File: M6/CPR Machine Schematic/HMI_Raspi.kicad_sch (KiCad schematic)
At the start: 15 parts, among them J10 Stop Button Port, J11 Go Button Port, J9 Laser Port, Q3 T2N7002BK,LM, Q6 T2N7002BK,LM, Q7 T2N7002BK,LM

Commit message: Final PCB
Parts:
- J9: footprint Connector_PinHeader_2.54mm:PinHeader_1x02_P2.54mm_Vertical -> TerminalBlock:TerminalBlock_MaiXu_MX126-5.0-02P_1x02_P5.00mm; digikey (none) -> 277-1667-ND; now in the parts list
- R6: value TEMP kOhm -> 0 Ohm; footprint Resistor_SMD:R_1206_3216Metric -> Resistor_SMD:R_1206_3216Metric_Pad1.30x1.75mm_HandSolder; digikey (none) -> RMCF1206ZT0R00CT-ND
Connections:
- net +5V: no longer R6.2
- net at J9.2 (Pin_2): now also R6.2; no longer R6.1
- new net +3.3V: R6.1
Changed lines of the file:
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@@
+	(wire
+		(pts
+			(xy 153.67 91.44) (xy 146.05 91.44)
+		)
+		(stroke
+			(width 0)
+			(type default)
+		)
+	)
+	(wire
+		(pts
+			(xy 78.74 63.5) (xy 81.28 63.5)
+		)
+		(stroke
+			(width 0)
+			(type default)
+		)
+	)
+	(wire
+		(pts
+			(xy 142.24 86.36) (xy 153.67 86.36)
+		)
+		(stroke
+			(width 0)
+			(type default)
+		)
+	)
+	(wire
+		(pts
+			(xy 129.54 59.69) (xy 130.81 59.69)
+		)
+		(stroke
+			(width 0)
+			(type default)
+		)
+	)
+	(wire
+		(pts
+			(xy 146.05 52.07) (xy 153.67 52.07)
+		)
+		(stroke
+			(width 0)
+			(type default)
+		)
+	)
+	(wire
+		(pts
+			(xy 88.9 63.5) (xy 90.17 63.5)
+		)
+		(stroke
+			(width 0)
+			(type default)
+		)
+	)
+	(wire
+		(pts
+			(xy 146.05 91.44) (xy 146.05 93.98)
+		)
+		(stroke
+			(width 0)
+			(type default)
+		)
+	)
+	(wire
+		(pts
+			(xy 78.74 64.77) (xy 78.74 63.5)
+		)
+		(stroke
+			(width 0)
+			(type default)
+		)
+	)
 	(wire
 		(pts
 			(xy 97.79 52.07) (xy 97.79 53.34)
-		)
-		(stroke
-			(width 0)
-			(type default)
-		)
-	)
-	(wire
-		(pts
-			(xy 153.67 91.44) (xy 146.05 91.44)
-		)
-		(stroke
-			(width 0)
-			(type default)
-		)
-	)
-	(wire
-		(pts
-			(xy 78.74 63.5) (xy 81.28 63.5)
-		)
-		(stroke
-			(width 0)
-			(type default)
-		)
-	)
-	(wire
-		(pts
-			(xy 142.24 86.36) (xy 153.67 86.36)
-		)
-		(stroke
-			(width 0)
-			(type default)
-		)
-	)
-	(wire
-		(pts
-			(xy 129.54 59.69) (xy 130.81 59.69)
-		)
-		(stroke
-			(width 0)
-			(type default)
-		)
-	)
-	(wire
-		(pts
-			(xy 146.05 52.07) (xy 153.67 52.07)
-		)
-		(stroke
-			(width 0)
-			(type default)
-		)
-	)
-	(wire
-		(pts
-			(xy 88.9 63.5) (xy 90.17 63.5)
-		)
-		(stroke
-			(width 0)
-			(type default)
-		)
-	)
-	(wire
-		(pts
-			(xy 146.05 91.44) (xy 146.05 93.98)
-		)
-		(stroke
-			(width 0)
-			(type default)
-		)
-	)
-	(wire
-		(pts
-			(xy 78.74 64.77) (xy 78.74 63.5)
 		)
 		(stroke
@@
 		(unit 1)
 		(exclude_from_sim no)
-		(in_bom no)
+		(in_bom yes)
 		(on_board yes)
 		(dnp no)
@@
 			)
 		)
-		(property "Footprint" "Connector_PinHeader_2.54mm:PinHeader_1x02_P2.54mm_Vertical"
+		(property "Footprint" "TerminalBlock:TerminalBlock_MaiXu_MX126-5.0-02P_1x02_P5.00mm"
 			(at 106.68 55.88 0)
 			(effects
@@
 			)
 		)
-		(property "Datasheet" "~"
+		(property "Datasheet" "https://mm.digikey.com/Volume0/opasdata/d220001/medias/docus/909/1935161.pdf"
 			(at 106.68 55.88 0)
 			(effects
@@
 		)
 		(property "Description" "Generic connector, single row, 01x02, script generated"
+			(at 106.68 55.88 0)
+			(effects
+				(font
+					(size 1.27 1.27)
+				)
+				(hide yes)
+			)
+		)
+		(property "digikey" "277-1667-ND"
 			(at 106.68 55.88 0)
 			(effects
@@
 	)
 	(symbol
+		(lib_id "Device:R_US")
+		(at 97.79 48.26 0)
+		(unit 1)
+		(exclude_from_sim no)
+		(in_bom no)
+		(on_board yes)
+		(dnp no)
+		(property "Reference" "R6"
+			(at 101.6 48.26 90)
+			(effects
+				(font
+					(size 1.27 1.27)
+				)
+			)
+		)
+		(property "Value" "0 Ohm"
+			(at 99.822 48.514 90)
+			(effects
+				(font
+					(size 1.27 1.27)
+				)
+			)
+		)
+		(property "Footprint" "Resistor_SMD:R_1206_3216Metric_Pad1.30x1.75mm_HandSolder"
+			(at 98.806 48.514 90)
+			(effects
+				(font
+					(size 1.27 1.27)
+				)
+				(hide yes)
+			)
+		)
+		(property "Datasheet" "~"
+			(at 97.79 48.26 0)
+			(effects
+				(font
+					(size 1.27 1.27)
+				)
+				(hide yes)
+			)
+		)
+		(property "Description" "Resistor, US symbol"
+			(at 97.79 48.26 0)
+			(effects
+				(font
+					(size 1.27 1.27)
+				)
+				(hide yes)
+			)
+		)
+		(property "digikey" "RMCF1206ZT0R00CT-ND"
+			(at 97.79 48.26 90)
+			(effects
+				(font
+					(size 1.27 1.27)
+				)
+				(hide yes)
+			)
+		)
+		(pin "2"
+		)
+		(pin "1"
+		)
+		(instances
+			(project "CPR Machine Schematic"
+				(path "/8991fc77-975f-4978-a089-6b2a5e33f59b/4742a649-a015-487c-b382-01878b0e2dd4"
+					(reference "R6")
+					(unit 1)
+				)
+			)
+		)
+	)
+	(symbol
+		(lib_id "power:+3.3V")
+		(at 97.79 44.45 0)
+		(unit 1)
+		(exclude_from_sim no)
+		(in_bom yes)
+		(on_board yes)
+		(dnp no)
+		(fields_autoplaced yes)
+		(property "Reference" "#PWR057"
+			(at 97.79 48.26 0)
+			(effects
+				(font
+					(size 1.27 1.27)
+				)
+				(hide yes)
+			)
+		)
+		(property "Value" "+3.3V"
+			(at 97.79 39.37 0)
+			(effects
+				(font
+					(size 1.27 1.27)
+				)
+			)
+		)
+		(property "Footprint" ""
+			(at 97.79 44.45 0)
+			(effects
+				(font
+					(size 1.27 1.27)
+				)
+				(hide yes)
+			)
+		)
+		(property "Datasheet" ""
+			(at 97.79 44.45 0)
+			(effects
+				(font
+					(size 1.27 1.27)
+				)
+				(hide yes)
+			)
+		)
+		(property "Description" "Power symbol creates a global label with name \"+3.3V\""
+			(at 97.79 44.45 0)
+			(effects
+				(font
+					(size 1.27 1.27)
+				)
+				(hide yes)
+			)
+		)
+		(pin "1"
+		)
+		(instances
+			(project ""
+				(path "/8991fc77-975f-4978-a089-6b2a5e33f59b/4742a649-a015-487c-b382-01878b0e2dd4"
+					(reference "#PWR057")
+					(unit 1)
+				)
+			)
+		)
+	)
+	(symbol
 		(lib_id "power:+5V")
 		(at 130.81 46.99 90)
@@
 	)
 	(symbol
-		(lib_id "Device:R_US")
-		(at 97.79 48.26 180)
-		(unit 1)
-		(exclude_from_sim no)
-		(in_bom no)
-		(on_board yes)
-		(dnp no)
-		(property "Reference" "R6"
-			(at 100.33 46.736 0)
-			(effects
-				(font
-					(size 1.27 1.27)
-				)
-			)
-		)
-		(property "Value" "TEMP kOhm"
-			(at 104.648 49.022 0)
-			(effects
-				(font
-					(size 1.27 1.27)
-				)
-			)
-		)
-		(property "Footprint" "Resistor_SMD:R_1206_3216Metric"
-			(at 96.774 48.006 90)
-			(effects
-				(font
-					(size 1.27 1.27)
-				)
-				(hide yes)
-			)
-		)
-		(property "Datasheet" "~"
-			(at 97.79 48.26 0)
-			(effects
-				(font
-					(size 1.27 1.27)
-				)
-				(hide yes)
-			)
-		)
-		(property "Description" "Resistor, US symbol"
-			(at 97.79 48.26 0)
-			(effects
-				(font
-					(size 1.27 1.27)
-				)
-				(hide yes)
-			)
-		)
-		(pin "2"
-		)
-		(pin "1"
-		)
-		(instances
-			(project "CPR Machine Schematic"
-				(path "/8991fc77-975f-4978-a089-6b2a5e33f59b/4742a649-a015-487c-b382-01878b0e2dd4"
-					(reference "R6")
-					(unit 1)
-				)
-			)
-		)
-	)
-	(symbol
 		(lib_id "power:GND")
 		(at 78.74 72.39 0)
@@
 					(unit 1)
 				)
-			)
-		)
-	)
-	(symbol
-		(lib_id "power:+5V")
-		(at 97.79 44.45 0)
-		(unit 1)
-		(exclude_from_sim no)
-		(in_bom yes)
-		(on_board yes)
-		(dnp no)
-		(fields_autoplaced yes)
-		(property "Reference" "#PWR057"
-			(at 97.79 48.26 0)
-			(effects
-				(font
-					(size 1.27 1.27)
-				)
-				(hide yes)
-			)
-		)
-		(property "Value" "+5V"
-			(at 97.79 39.37 0)
-			(effects
-				(font
-					(size 1.27 1.27)
-				)
-			)
-		)
-		(property "Footprint" ""
-			(at 97.79 44.45 0)
-			(effects
-				(font
-					(size 1.27 1.27)
-				)
-				(hide yes)
-			)
-		)
-		(property "Datasheet" ""
-			(at 97.79 44.45 0)
-			(effects
-				(font
-					(size 1.27 1.27)
-				)
-				(hide yes)
-			)
-		)
-		(property "Description" "Power symbol creates a global label with name \"+5V\""
-			(at 97.79 44.45 0)
-			(effects
-				(font
-					(size 1.27 1.27)
-				)
-				(hide yes)
-			)
-		)
-		(pin "1"
-		)
-		(instances
-			(project ""
-				(path "/8991fc77-975f-4978-a089-6b2a5e33f59b/4742a649-a015-487c-b382-01878b0e2dd4"
-					(reference "#PWR057")
-					(unit 1)
-				)

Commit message: Board V2 Final
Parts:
- J9, R15, R5: now left out of the parts list
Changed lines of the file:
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@@
+			)
+		)
+		(property "Notes" ""
+			(at 158.75 49.53 0)
+			(effects
+				(font
+					(size 1.27 1.27)
+				)
+				(hide yes)
 			)
 		)
@@
 		(unit 1)
 		(exclude_from_sim no)
-		(in_bom yes)
+		(in_bom no)
 		(on_board yes)
 		(dnp no)
@@
 			)
 		)
+		(property "Notes" ""
+			(at 106.68 55.88 0)
+			(effects
+				(font
+					(size 1.27 1.27)
+				)
+				(hide yes)
+			)
+		)
 		(pin "2"
 		)
@@
 		(property "Description" "Resistor, US symbol"
 			(at 134.62 59.69 0)
+			(effects
+				(font
+					(size 1.27 1.27)
+				)
+				(hide yes)
+			)
+		)
+		(property "Notes" ""
+			(at 134.62 59.69 90)
 			(effects
 				(font
@@
 			)
 		)
+		(property "Notes" ""
+			(at 143.51 99.06 0)
+			(effects
+				(font
+					(size 1.27 1.27)
+				)
+				(hide yes)
+			)
+		)
 		(pin "2"
 		)
@@
 			)
 		)
+		(property "Notes" ""
+			(at 78.74 68.58 0)
+			(effects
+				(font
+					(size 1.27 1.27)
+				)
+				(hide yes)
+			)
+		)
 		(pin "2"
 		)
@@
 		(unit 1)
 		(exclude_from_sim no)
-		(in_bom yes)
+		(in_bom no)
 		(on_board yes)
 		(dnp no)
@@
 			)
 		)
+		(property "Notes" ""
+			(at 134.62 46.99 90)
+			(effects
+				(font
+					(size 1.27 1.27)
+				)
+				(hide yes)
+			)
+		)
 		(pin "2"
 		)
@@
 		(unit 1)
 		(exclude_from_sim no)
-		(in_bom yes)
+		(in_bom no)
 		(on_board yes)
 		(dnp no)
@@
 			)
 		)
+		(property "Notes" ""
+			(at 138.43 86.36 90)
+			(effects
+				(font
+					(size 1.27 1.27)
+				)
+				(hide yes)
+			)
+		)
 		(pin "2"
 		)
@@
 		)
 		(property "digikey" "RMCF1206ZT0R00CT-ND"
+			(at 97.79 48.26 90)
+			(effects
+				(font
+					(size 1.27 1.27)
+				)
+				(hide yes)
+			)
+		)
+		(property "Notes" ""
 			(at 97.79 48.26 90)
 			(effects
@@
 			)
 		)
+		(property "Notes" ""
+			(at 85.09 63.5 90)
+			(effects
+				(font
+					(size 1.27 1.27)
+				)
+				(hide yes)
+			)
+		)
 		(pin "2"
 		)
@@
 			)
 		)
+		(property "Notes" ""
+			(at 134.62 99.06 90)
+			(effects
+				(font
+					(size 1.27 1.27)
+				)
+				(hide yes)
+			)
+		)
 		(pin "2"
 		)
@@
 		)
 		(property "Description" "Resistor, US symbol"
+			(at 129.54 63.5 0)
+			(effects
+				(font
+					(size 1.27 1.27)
+				)
+				(hide yes)
+			)
+		)
+		(property "Notes" ""
 			(at 129.54 63.5 0)
 			(effects
@@
 			)
 		)
+		(property "Notes" ""
+			(at 95.25 63.5 0)
+			(effects
+				(font
+					(size 1.27 1.27)
+				)
+				(hide yes)
+			)
+		)
 		(pin "2"
 		)
@@
 			)
 		)
+		(property "Notes" ""
+			(at 143.51 59.69 0)
+			(effects
+				(font
+					(size 1.27 1.27)
+				)
+				(hide yes)
+			)
+		)
 		(pin "2"
 		)
@@
 			)
 		)
+		(property "Notes" ""
+			(at 128.27 102.87 0)
+			(effects
+				(font
+					(size 1.27 1.27)
+				)
+				(hide yes)
+			)
+		)
 		(pin "2"
 		)
@@
 			(at 158.75 88.9 0)
 			(effects
+				(font
+					(size 1.27 1.27)
+				)
+				(hide yes)
+			)
+		)
+		(property "Notes" ""
+			(at 158.75 88.9 0)
+			(effects

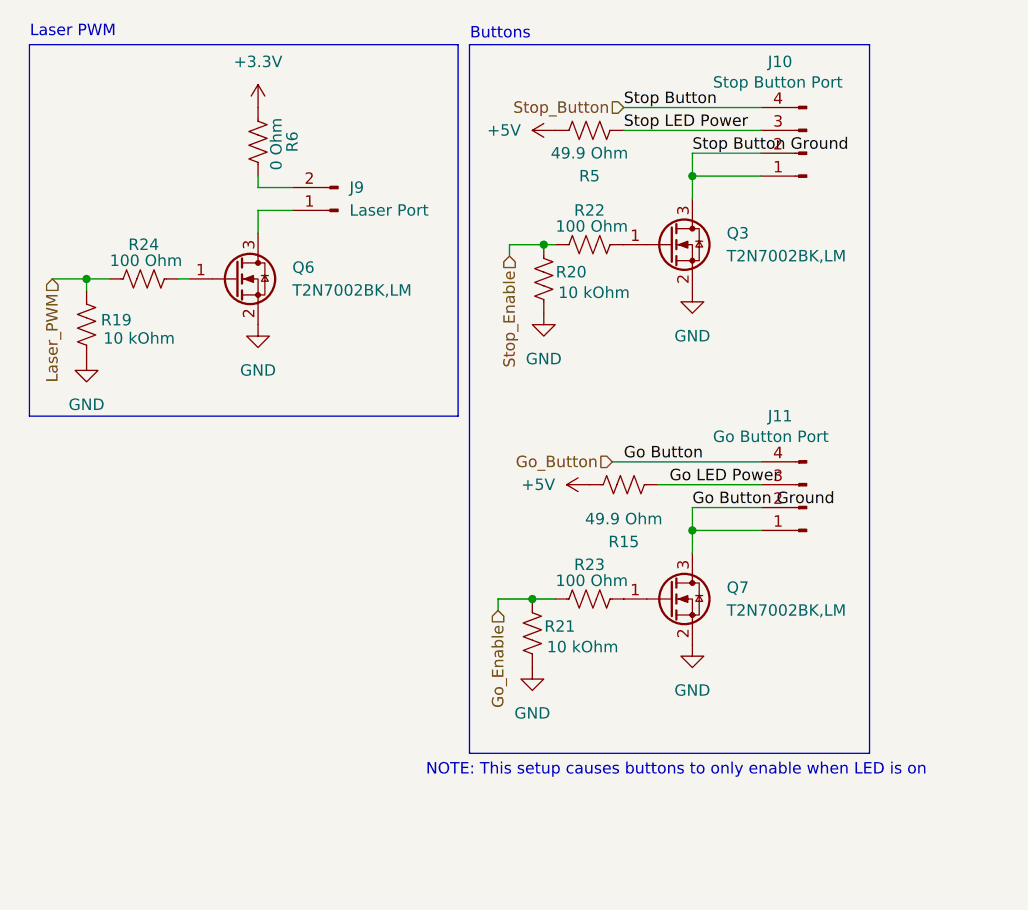
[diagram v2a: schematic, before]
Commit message: Voltage readout, MUX, Debouncing Caps
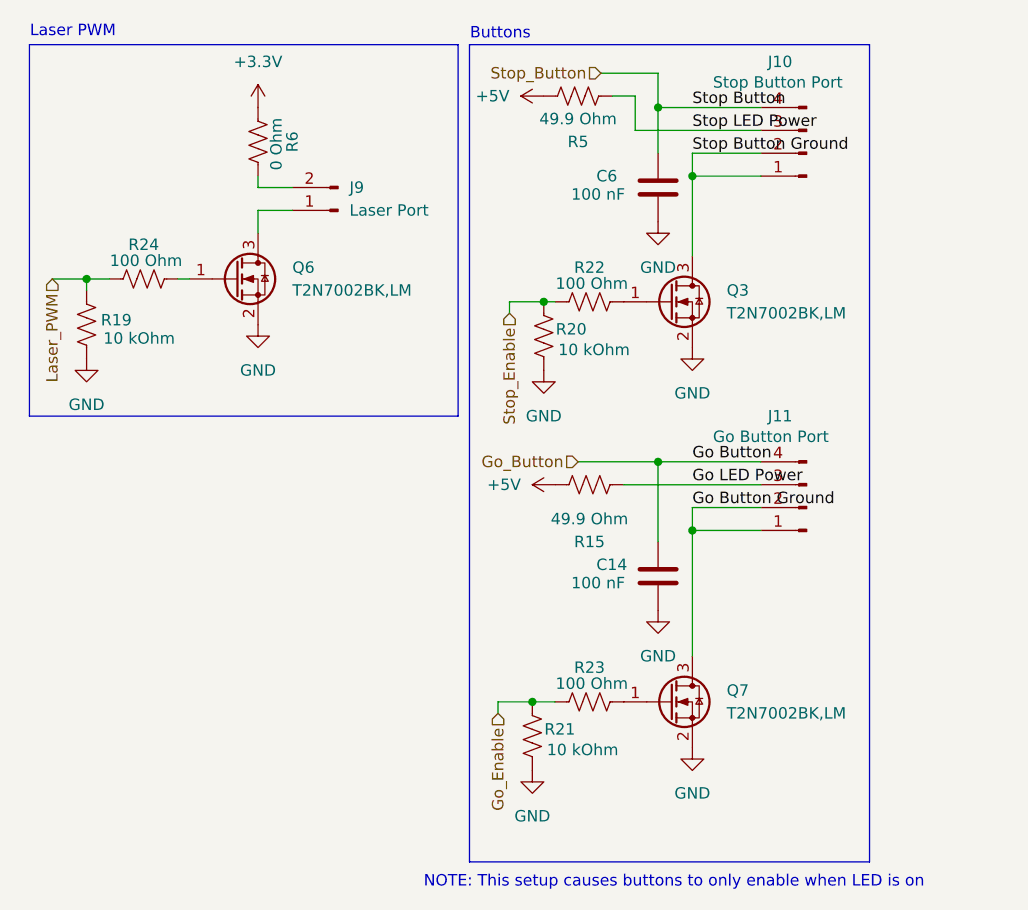
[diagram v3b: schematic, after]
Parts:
- added C14, C6: 100 nF, symbol Device:C
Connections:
- net GND: now also C14.1, C6.1
- net Go_Button: now also C14.2
- net Stop_Button: now also C6.2
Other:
- moved on the sheet: Q3, Q7, R15, R20, R21, R22, R23, R5
